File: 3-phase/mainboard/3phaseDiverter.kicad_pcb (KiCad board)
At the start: 2 copper layers, 144.8 x 120.6 mm, 100 parts, among them CN9 SMA, IC1 ATmega328-P, IC2 LM358, J0 FTDI, J1 RESET, J10 D10, J11 D11, J12 D12, J13 D13, J14 +5V, J15 +5V, J2 D2, J20 UnregDC, J3 D3, J30 regDC, J4 D4, J5 D5, J6 D6, J7 D7, J8 D8, J9 D9, X1 16MHz

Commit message: Some tuning
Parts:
- IC1: footprint Package_DIP:DIP-28_W7.62mm_Socket_LongPads -> PCM_Package_DIP_AKL:DIP-28_W7.62mm_Socket_LongPads
- IC2: footprint Package_DIP:DIP-8_W7.62mm_Socket_LongPads -> PCM_Package_DIP_AKL:DIP-8_W7.62mm_Socket_LongPads
- moved C6 0.26 mm to (90.3, 38.8)
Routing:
- net /D2: track 35.6 -> 36.3 mm

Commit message: Some updates
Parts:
- added REF**: Symbol_HighVoltage_Type2_Silk_VerySmall, Library:Symbol_HighVoltage_Type2_Silk_VerySmall, F.Cu at (108.7, 121.4)
- added REF**: Symbol_HighVoltage_Type2_Silk_VerySmall, Library:Symbol_HighVoltage_Type2_Silk_VerySmall, F.Cu at (63.3, 121.4)
- added REF**: Symbol_HighVoltage_Type2_Silk_VerySmall, Library:Symbol_HighVoltage_Type2_Silk_VerySmall, B.Cu at (135.2, 124.5)
- added REF**: Symbol_HighVoltage_Type2_Silk_VerySmall, Library:Symbol_HighVoltage_Type2_Silk_VerySmall, B.Cu at (87.0, 124.5)
- added REF**: Symbol_HighVoltage_Type2_Silk_VerySmall, Library:Symbol_HighVoltage_Type2_Silk_VerySmall, B.Cu at (38.6, 124.5)
- added kibuzzard-6431D11C: G***, kibuzzard-6431D11C, F.Cu at (69.2, 74.1)
- added kibuzzard-64EB6544: G***, kibuzzard-64EB6544, F.Cu at (68.5, 78.4)
- moved G*** 7.84 mm to (46.6, 69.1)

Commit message: Some tuning
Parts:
- renumbered C9 to C10, C10 to C11, C11 to C20, C12 to C21, C8 to C6, C6 to C7, C7 to C8, C13 to C9
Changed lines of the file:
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@@
     (property "ki_description" "Unpolarized capacitor")
     (property "ki_keywords" "cap capacitor")
-    (fp_text reference "C13" (at 2.5 -2.159 -90) (layer "F.SilkS")
+    (fp_text reference "C9" (at 2.5 -2.159 90) (layer "F.SilkS")
         (effects (font (size 1 1) (thickness 0.15)))
     )
-    (fp_text value "100nF" (at 2.5 2.5 -90) (layer "F.Fab") hide
+    (fp_text value "100nF" (at 2.5 2.5 90) (layer "F.Fab") hide
         (effects (font (size 1 1) (thickness 0.15)))
     )
-    (fp_text user "${REFERENCE}" (at 2.5 0 -90) (layer "F.Fab")
+    (fp_text user "${REFERENCE}" (at 2.5 0 90) (layer "F.Fab")
         (effects (font (size 0.94 0.94) (thickness 0.141)))
     )
@@
     (property "ki_description" "Unpolarized capacitor")
     (property "ki_keywords" "cap capacitor")
-    (fp_text reference "C12" (at 2.5 -2.5 -90) (layer "F.SilkS")
+    (fp_text reference "C21" (at 2.5 -2.5 90) (layer "F.SilkS")
         (effects (font (size 1 1) (thickness 0.15)))
     )
-    (fp_text value "100nF" (at 2.5 2.5 -90) (layer "F.Fab") hide
+    (fp_text value "100nF" (at 2.5 2.5 90) (layer "F.Fab") hide
         (effects (font (size 1 1) (thickness 0.15)))
     )
-    (fp_text user "${REFERENCE}" (at 2.5 0 -90) (layer "F.Fab")
+    (fp_text user "${REFERENCE}" (at 2.5 0 90) (layer "F.Fab")
         (effects (font (size 0.94 0.94) (thickness 0.141)))
     )
@@
     (property "ki_description" "Unpolarized capacitor")
     (property "ki_keywords" "cap capacitor")
-    (fp_text reference "C6" (at 2.5 -2.5 180) (layer "F.SilkS")
+    (fp_text reference "C7" (at 2.5 -2.5 180) (layer "F.SilkS")
         (effects (font (size 1 1) (thickness 0.15)))
     )
@@
     (property "ki_keywords" "connector")
     (attr through_hole)
-    (fp_text reference "PWR1" (at 10.16 4.8655) (layer "F.SilkS") hide
+    (fp_text reference "PWR1" (at 5.08 7.1261) (layer "F.SilkS")
         (effects (font (size 1 1) (thickness 0.15)))
     )
@@
     (property "ki_description" "Unpolarized capacitor")
     (property "ki_keywords" "cap capacitor")
-    (fp_text reference "C7" (at 2.5 2.159 90) (layer "F.SilkS")
+    (fp_text reference "C8" (at 2.5 2.159 90) (layer "F.SilkS")
         (effects (font (size 1 1) (thickness 0.15)))
     )
@@
     (property "ki_keywords" "cap capacitor")
     (attr through_hole)
-    (fp_text reference "C11" (at 3.918999 0 90) (layer "F.SilkS")
+    (fp_text reference "C20" (at 3.918999 0 90) (layer "F.SilkS")
         (effects (font (size 1 1) (thickness 0.15)))
     )
@@
     (property "ki_keywords" "connector")
     (attr through_hole)
-    (fp_text reference "PWR2" (at 10.16 4.8655) (layer "F.SilkS") hide
+    (fp_text reference "PWR2" (at 5.08 7.1261) (layer "F.SilkS")
         (effects (font (size 1 1) (thickness 0.15)))
     )
@@
     (property "ki_description" "Unpolarized capacitor")
     (property "ki_keywords" "cap capacitor")
-    (fp_text reference "C10" (at 1.233 -2.1082) (layer "F.SilkS")
+    (fp_text reference "C11" (at 1.233 -2.1082) (layer "F.SilkS")
         (effects (font (size 1 1) (thickness 0.15)))
     )
@@
     (property "ki_keywords" "connector")
     (attr through_hole)
-    (fp_text reference "PWR3" (at 10.16 4.8655) (layer "F.SilkS") hide
+    (fp_text reference "PWR3" (at 5.08 7.1261) (layer "F.SilkS")
         (effects (font (size 1 1) (thickness 0.15)))
     )
@@
     (property "ki_description" "Unpolarized capacitor")
     (property "ki_keywords" "cap capacitor")
-    (fp_text reference "C9" (at 1.267 2.1844 180) (layer "F.SilkS")
+    (fp_text reference "C10" (at 1.267 2.1844 180) (layer "F.SilkS")
         (effects (font (size 1 1) (thickness 0.15)))
     )
@@
     (property "ki_description" "Unpolarized capacitor")
     (property "ki_keywords" "cap capacitor")
-    (fp_text reference "C8" (at 2.5 -2.5 180) (layer "F.SilkS")
+    (fp_text reference "C6" (at 2.5 -2.5 180) (layer "F.SilkS")
         (effects (font (size 1 1) (thickness 0.15)))
     )

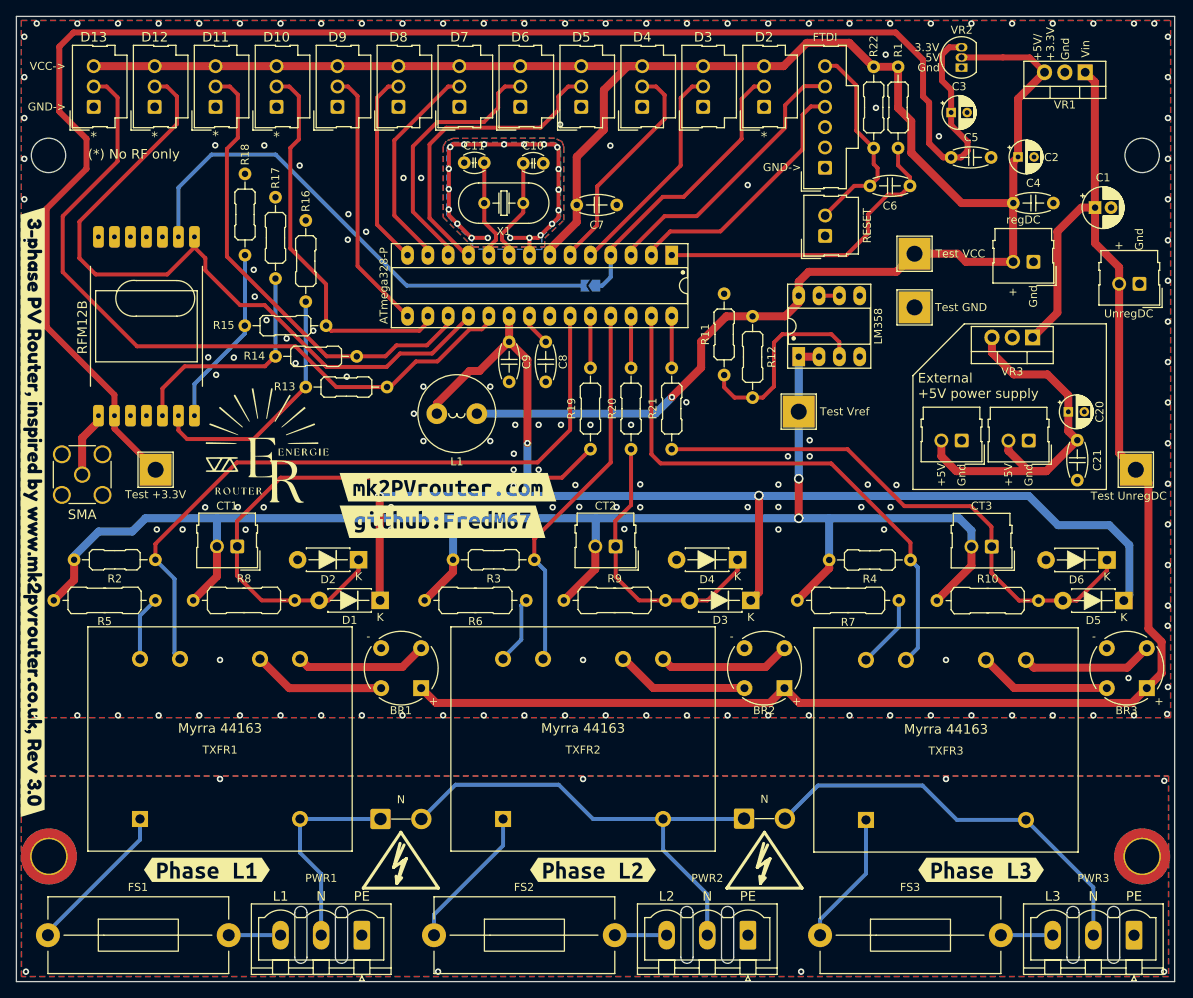
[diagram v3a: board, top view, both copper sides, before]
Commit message: Fix wrong pad & tuning
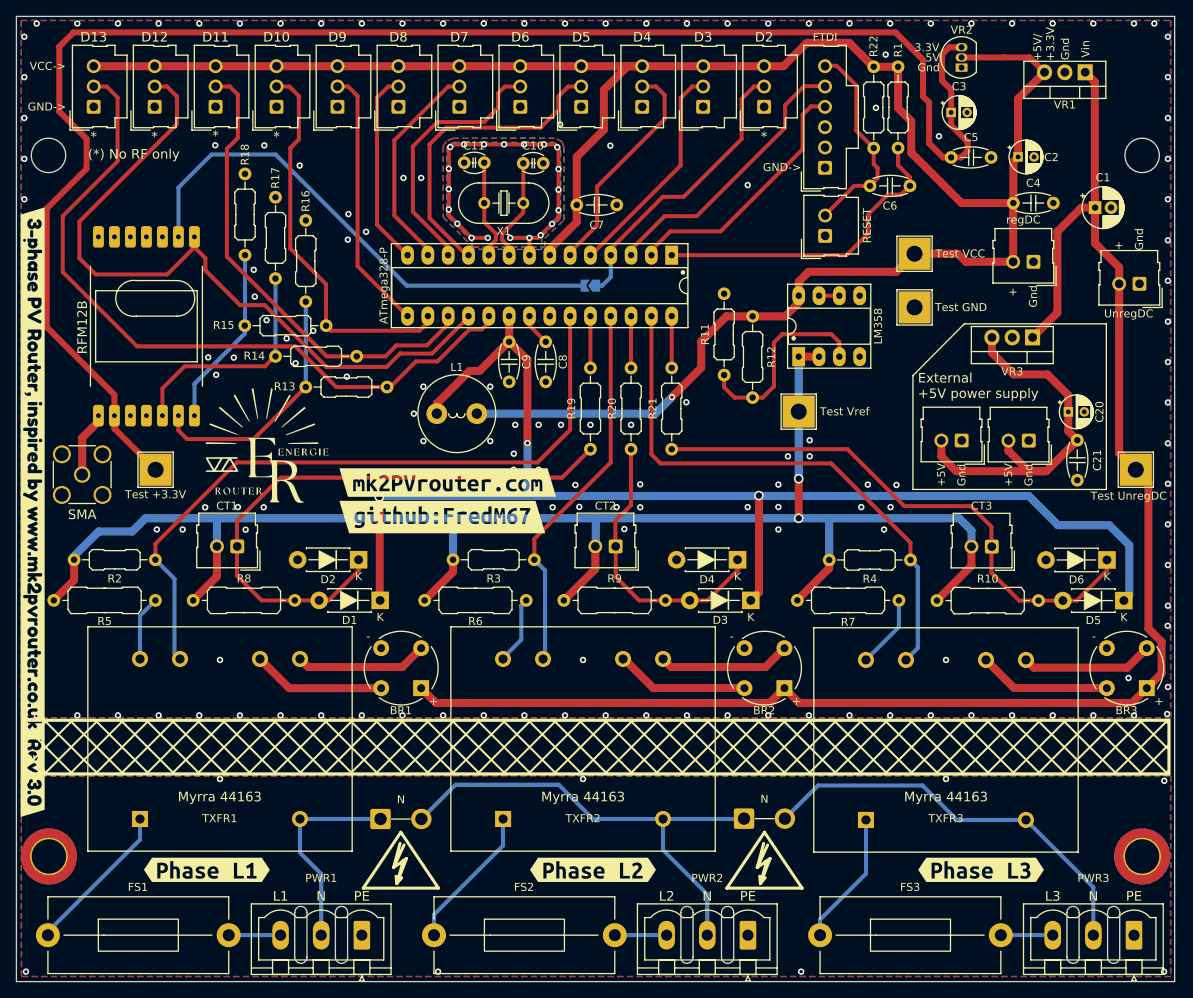
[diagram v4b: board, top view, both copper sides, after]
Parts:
- moved kibuzzard-6431D11C 0.58 mm to (69.2, 73.5)
- moved kibuzzard-64EB6544 0.58 mm to (68.5, 77.8)
- renumbered REF** to REF1, REF** to REF2, REF** to REF3, REF** to REF4
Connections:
- REF2 pad 1: (no net) -> Earth
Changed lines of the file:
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@@
     (tags "mounting hole 4.3mm no annular m4 din965")
     (attr board_only exclude_from_pos_files exclude_from_bom)
-    (fp_text reference "REF**" (at 0 -4.75) (layer "F.SilkS") hide
+    (fp_text reference "REF4" (at 0 -4.75) (layer "F.SilkS") hide
         (effects (font (size 1 1) (thickness 0.15)))
     )
@@
     (descr "Mounting Hole 4.3mm, M4, ISO14580")
     (tags "mounting hole 4.3mm m4 iso14580")
-    (attr exclude_from_pos_files exclude_from_bom)
-    (fp_text reference "REF**" (at 0 -4.5) (layer "F.SilkS") hide
+    (attr board_only exclude_from_pos_files exclude_from_bom)
+    (fp_text reference "REF1" (at 0 -4.5) (layer "F.SilkS") hide
         (effects (font (size 1 1) (thickness 0.15)))
     )
@@
   )
   (footprint "kibuzzard-64EB6544" (layer "F.Cu")
-    (at 68.5038 78.4098)
+    (at 68.4784 77.8256)
     (descr "Generated with KiBuzzard")
     (tags "kb_params=eyJBbGlnbm1lbnRDaG9pY2UiOiAiQ2VudGVyIiwgIkNhcExlZnRDaG9pY2UiOiAiXFwiLCAiQ2FwUmlnaHRDaG9pY2UiOiAiXFwiLCAiRm9udENvbWJvQm94IjogIlVidW50dU1vbm8tQiIsICJIZWlnaHRDdHJsIjogIjIiLCAiTGF5ZXJDb21ib0JveCI6ICJGLlNpbGtTIiwgIk11bHRpTGluZVRleHQiOiAiZ2l0aHViOkZyZWRNNjciLCAiUGFkZGluZ0JvdHRvbUN0cmwiOiAiNSIsICJQYWRkaW5nTGVmdEN0cmwiOiAiNSIsICJQYWRkaW5nUmlnaHRDdHJsIjogIjUiLCAiUGFkZGluZ1RvcEN0cmwiOiAiNSIsICJXaWR0aEN0cmwiOiAiIn0=")
@@
     (descr "Mounting Hole 4.3mm, M4, ISO14580")
     (tags "mounting hole 4.3mm m4 iso14580")
-    (attr exclude_from_pos_files exclude_from_bom)
-    (fp_text reference "REF**" (at 0 -4.5) (layer "F.SilkS") hide
+    (attr board_only exclude_from_pos_files exclude_from_bom)
+    (fp_text reference "REF2" (at 0 -4.5) (layer "F.SilkS") hide
         (effects (font (size 1 1) (thickness 0.15)))
     )
@@
       (stroke (width 0.05) (type solid)) (fill none) (layer "F.CrtYd"))
     (pad "1" thru_hole circle (at 0 0) (size 4.7 4.7) (drill 4.3) (layers "*.Cu" "*.Mask"))
-    (pad "1" connect circle (at 0 0) (size 7 7) (layers "F.Cu" "F.Mask"))
+    (pad "1" connect circle (at 0 0) (size 7 7) (layers "F.Cu" "F.Mask")
+      (net 45 "Earth"))
     (pad "1" connect circle (at 0 0) (size 7 7) (layers "B.Cu" "B.Mask"))
   )
@@
     (tags "mounting hole 4.3mm no annular m4 din965")
     (attr board_only exclude_from_pos_files exclude_from_bom)
-    (fp_text reference "REF**" (at 0 -4.75) (layer "F.SilkS") hide
+    (fp_text reference "REF3" (at 0 -4.75) (layer "F.SilkS") hide
         (effects (font (size 1 1) (thickness 0.15)))
     )
@@
     (property "Sheetname" "")
     (attr through_hole)
-    (fp_text reference "TXFR3" (at 8.636125 9.999875 180) (layer "F.SilkS")
+    (fp_text reference "TXFR3" (at 0.180401 9.999875 180) (layer "F.SilkS")
         (effects (font (size 1 1) (thickness 0.15)))
     )
-    (fp_text value "Myrra 44163" (at 11.336125 9.999875 180) (layer "F.SilkS")
+    (fp_text value "Myrra 44163" (at 2.880401 9.999875 180) (layer "F.SilkS")
         (effects (font (size 1.2 1.2) (thickness 0.15)))
     )
@@
     (descr "Symbol, High Voltage, Type 2, SilkScreen, Very Small,")
     (tags "Symbol, High Voltage, Type 2, SilkScreen, Very Small,")
-    (attr exclude_from_pos_files exclude_from_bom)
+    (attr board_only exclude_from_pos_files exclude_from_bom)
     (fp_text reference "REF**" (at -0.127 -5.715) (layer "F.SilkS") hide
         (effects (font (size 1 1) (thickness 0.15)))
@@
     (property "Sheetname" "")
     (attr through_hole)
-    (fp_text reference "TXFR2" (at 8.636125 9.999875 180) (layer "F.SilkS")
+    (fp_text reference "TXFR2" (at 0.061 9.999875 180) (layer "F.SilkS")
         (effects (font (size 1 1) (thickness 0.15)))
     )
-    (fp_text value "Myrra 44163" (at 11.336125 9.999875 180) (layer "F.SilkS")
+    (fp_text value "Myrra 44163" (at 2.761 9.999875 180) (layer "F.SilkS")
         (effects (font (size 1.2 1.2) (thickness 0.15)))
     )
@@
   )
   (footprint "kibuzzard-6431D11C" (layer "F.Cu")
-    (at 69.184838 74.0918)
+    (at 69.159438 73.5076)
     (descr "Generated with KiBuzzard")
     (tags "kb_params=eyJBbGlnbm1lbnRDaG9pY2UiOiAiQ2VudGVyIiwgIkNhcExlZnRDaG9pY2UiOiAiXFwiLCAiQ2FwUmlnaHRDaG9pY2UiOiAiXFwiLCAiRm9udENvbWJvQm94IjogIlVidW50dU1vbm8tQiIsICJIZWlnaHRDdHJsIjogIjIiLCAiTGF5ZXJDb21ib0JveCI6ICJGLlNpbGtTIiwgIk11bHRpTGluZVRleHQiOiAibWsyUFZyb3V0ZXIuY29tIiwgIlBhZGRpbmdCb3R0b21DdHJsIjogIjUiLCAiUGFkZGluZ0xlZnRDdHJsIjogIjUiLCAiUGFkZGluZ1JpZ2h0Q3RybCI6ICI1IiwgIlBhZGRpbmdUb3BDdHJsIjogIjUiLCAiV2lkdGhDdHJsIjogIiJ9")
@@
     (descr "Symbol, High Voltage, Type 2, SilkScreen, Very Small,")
     (tags "Symbol, High Voltage, Type 2, SilkScreen, Very Small,")
-    (attr exclude_from_pos_files exclude_from_bom)
+    (attr board_only exclude_from_pos_files exclude_from_bom)
     (fp_text reference "REF**" (at -0.127 -5.715) (layer "F.SilkS") hide
         (effects (font (size 1 1) (thickness 0.15)))
@@
     (property "Sheetname" "")
     (attr through_hole)
-    (fp_text reference "TXFR1" (at 8.636125 9.999875 180) (layer "F.SilkS")
+    (fp_text reference "TXFR1" (at 0.061 9.974475 180) (layer "F.SilkS")
         (effects (font (size 1 1) (thickness 0.15)))
     )
-    (fp_text value "Myrra 44163" (at 11.336125 9.999875 180) (layer "F.SilkS")
+    (fp_text value "Myrra 44163" (at 2.761 9.974475 180) (layer "F.SilkS")
         (effects (font (size 1.2 1.2) (thickness 0.15)))
     )
@@
     (property "ki_keywords" "inductor choke coil reactor magnetic")
     (attr through_hole)
-    (fp_text reference "L1" (at 2.5 -6 180) (layer "F.SilkS")
+    (fp_text reference "L1" (at 2.500001 5.7912 180) (layer "F.SilkS")
         (effects (font (size 1 1) (thickness 0.15)))
     )
@@
     (descr "Symbol, High Voltage, Type 2, SilkScreen, Very Small,")
     (tags "Symbol, High Voltage, Type 2, SilkScreen, Very Small,")
-    (attr exclude_from_pos_files exclude_from_bom)
+    (attr board_only exclude_from_pos_files exclude_from_bom)
     (fp_text reference "REF**" (at -0.127 5.715) (layer "B.SilkS") hide
         (effects (font (size 1 1) (thickness 0.15)) (justify mirror))
@@
     (descr "Symbol, High Voltage, Type 2, SilkScreen, Very Small,")
     (tags "Symbol, High Voltage, Type 2, SilkScreen, Very Small,")
-    (attr exclude_from_pos_files exclude_from_bom)
+    (attr board_only exclude_from_pos_files exclude_from_bom)
     (fp_text reference "REF**" (at -0.127 5.715) (layer "B.SilkS") hide
         (effects (font (size 1 1) (thickness 0.15)) (justify mirror))
@@
     (descr "Symbol, High Voltage, Type 2, SilkScreen, Very Small,")
     (tags "Symbol, High Voltage, Type 2, SilkScreen, Very Small,")
-    (attr exclude_from_pos_files exclude_from_bom)
+    (attr board_only exclude_from_pos_files exclude_from_bom)
     (fp_text reference "REF**" (at -0.127 5.715) (layer "B.SilkS") hide
         (effects (font (size 1 1) (thickness 0.15)) (justify mirror))
@@
     (polygon
       (pts
-        (xy 159.258 135.255)
+        (xy 159.512 135.255)
         (xy 15.875 135.255)
         (xy 15.8496 110.1852)
-        (xy 159.258 110.1852)
+        (xy 159.512 110.1598)
       )
     )
@@
       )
     )
+  )
+  (zone (net 0) (net_name "") (layers "*.SilkS") (hatch edge 0.5)
+    (connect_pads (clearance 0))
+    (min_thickness 0.25) (filled_areas_thickness no)
+    (fill yes (mode hatch) (thermal_gap 0.5) (thermal_bridge_width 0.5)
+      (hatch_thickness 0.25) (hatch_gap 2) (hatch_orientation 45)
+      (hatch_border_algorithm hatch_thickness) (hatch_min_hole_area 0.3))
+    (polygon
+      (pts
+        (xy 15.8496 103.0224)
+        (xy 15.8496 110.1344)
+        (xy 159.512 110.1344)
+        (xy 159.512 103.0224)
+      )
+    )

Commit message: Some tuning
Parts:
- removed kibuzzard-64C01F08: G***, kibuzzard-64C01F08
- added kibuzzard-65314627: G***, kibuzzard-65314627, F.Cu at (17.3, 77.2)
- moved C7 6.04 mm to (84.7, 36.5), turned to -90 degrees
- moved L1 2.88 mm to (73.4, 67.7), turned to 90 degrees
- moved C11 2.01 mm to (71.2, 35.5)
- moved C10 1.93 mm to (81.1, 35.5)
- moved C9 1.91 mm to (78.7, 55.9)
- moved X1 1.32 mm to (78.6, 39.9)
- moved TP3 1.27 mm to (127.5, 52.9)
- moved C8 0.64 mm to (82.0, 60.9)
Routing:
- net AVCC: track 166.9 -> 173.9 mm, vias 3 -> 2
- net GND: track 46.4 -> 39.8 mm
- net Net-(IC1-PB7/XTAL2/TOSC): track 12.5 -> 10.4 mm
- net Net-(IC1-PB6/XTAL1/TOSC1): track 12.9 -> 10.9 mm
- net VCC: track 274.9 -> 276.5 mm, vias 1 -> 0
- net /D5: track 39.0 -> 37.5 mm
- net Net-(IC1-AREF): track 4.06 -> 5.08 mm
- net /D6: track 33.0 -> 32.5 mm

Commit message: Tuning
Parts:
- added G***: LOGO, LOGO, B.Cu at (122.0, 73.6)
- added kibuzzard-6431D11C: G***, kibuzzard-6431D11C, B.Cu at (68.0, 73.4)
- added kibuzzard-64EB6544: G***, kibuzzard-64EB6544, B.Cu at (68.5, 78.0)
